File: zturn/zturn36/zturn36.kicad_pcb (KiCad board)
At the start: 4 copper layers, 189.9 x 136.5 mm, 61 parts, among them J11 Conn_02x40_Odd_Even, J12 Conn_02x40_Odd_Even, J5V1 Conn_01x03, Q1 SSM6N15AFU, Q2 SSM6N15AFU, Q3 SSM6N15AFU, Q4 SSM6N15AFU, Q5 SSM6N15AFU, Q6 SSM6N15AFU, Q7 SSM6N15AFU, Q8 SSM6N15AFU, Q9 SSM6N15AFU, U1 74AXP4T245, U10 74AXP4T245, U11 74AXP4T245, U12 74AXP4T245, U13 74AXP4T245, U14 LM3940_TO220, U2 74AXP4T245, U3 74AXP4T245, U8 74AXP4T245, U9 74AXP4T245

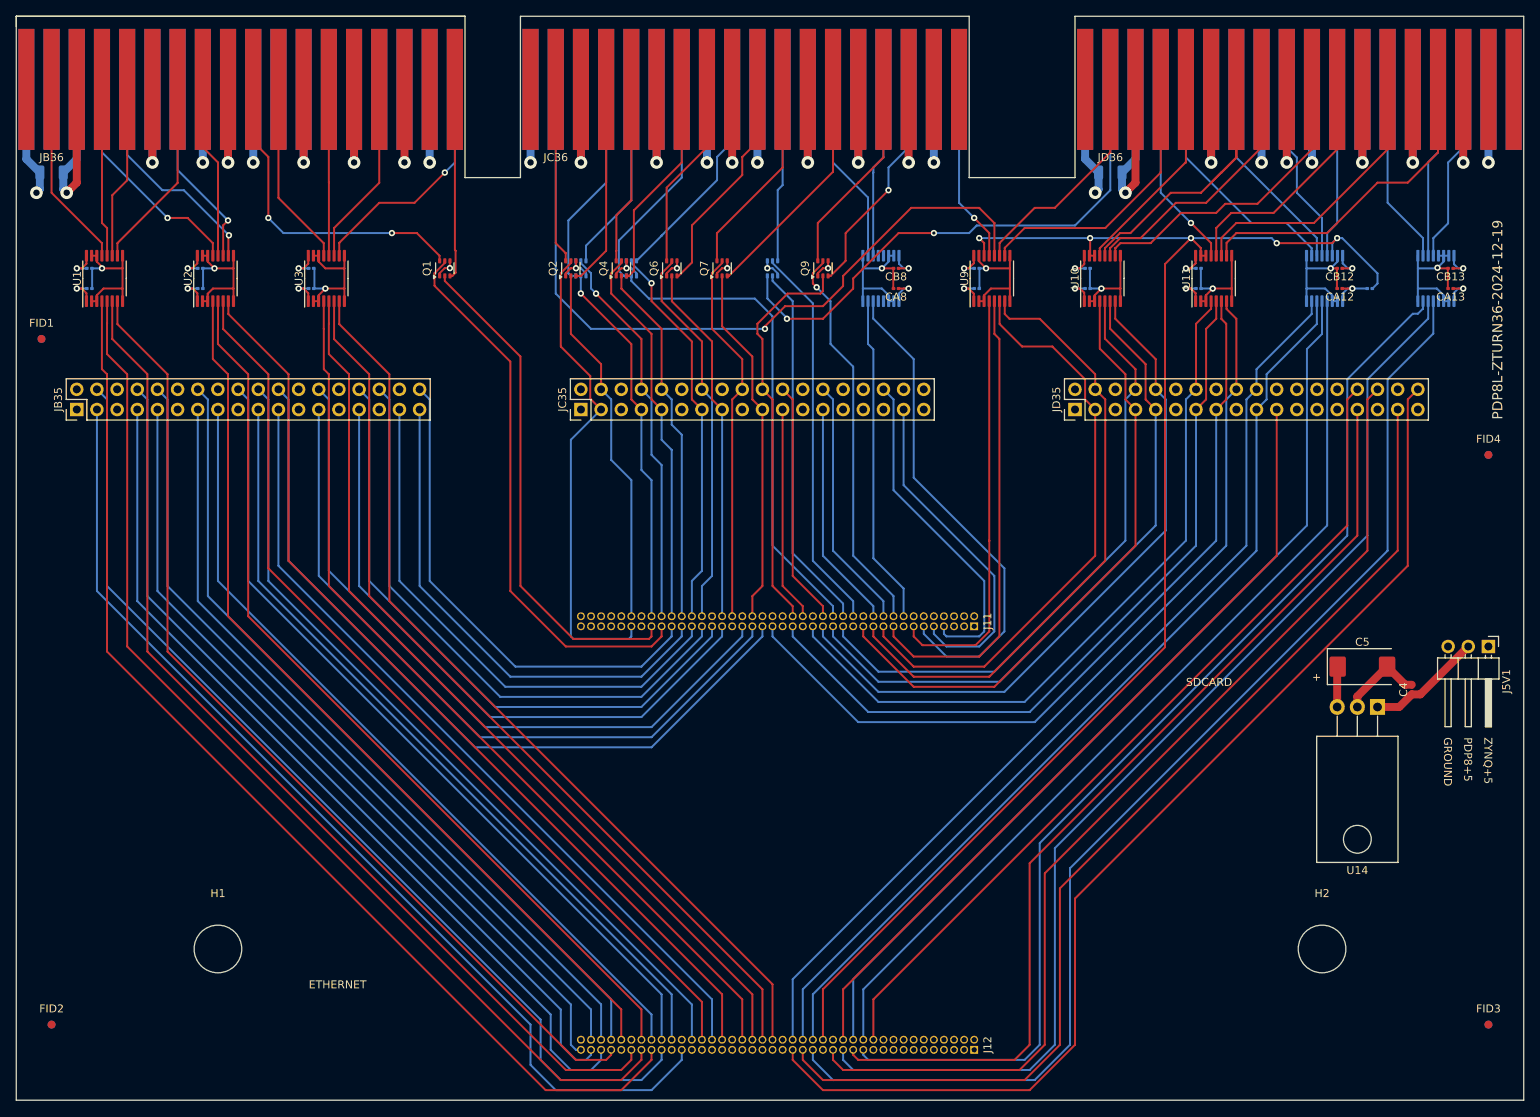
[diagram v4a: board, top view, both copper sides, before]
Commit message: update signals and zturn pcbs with pullups
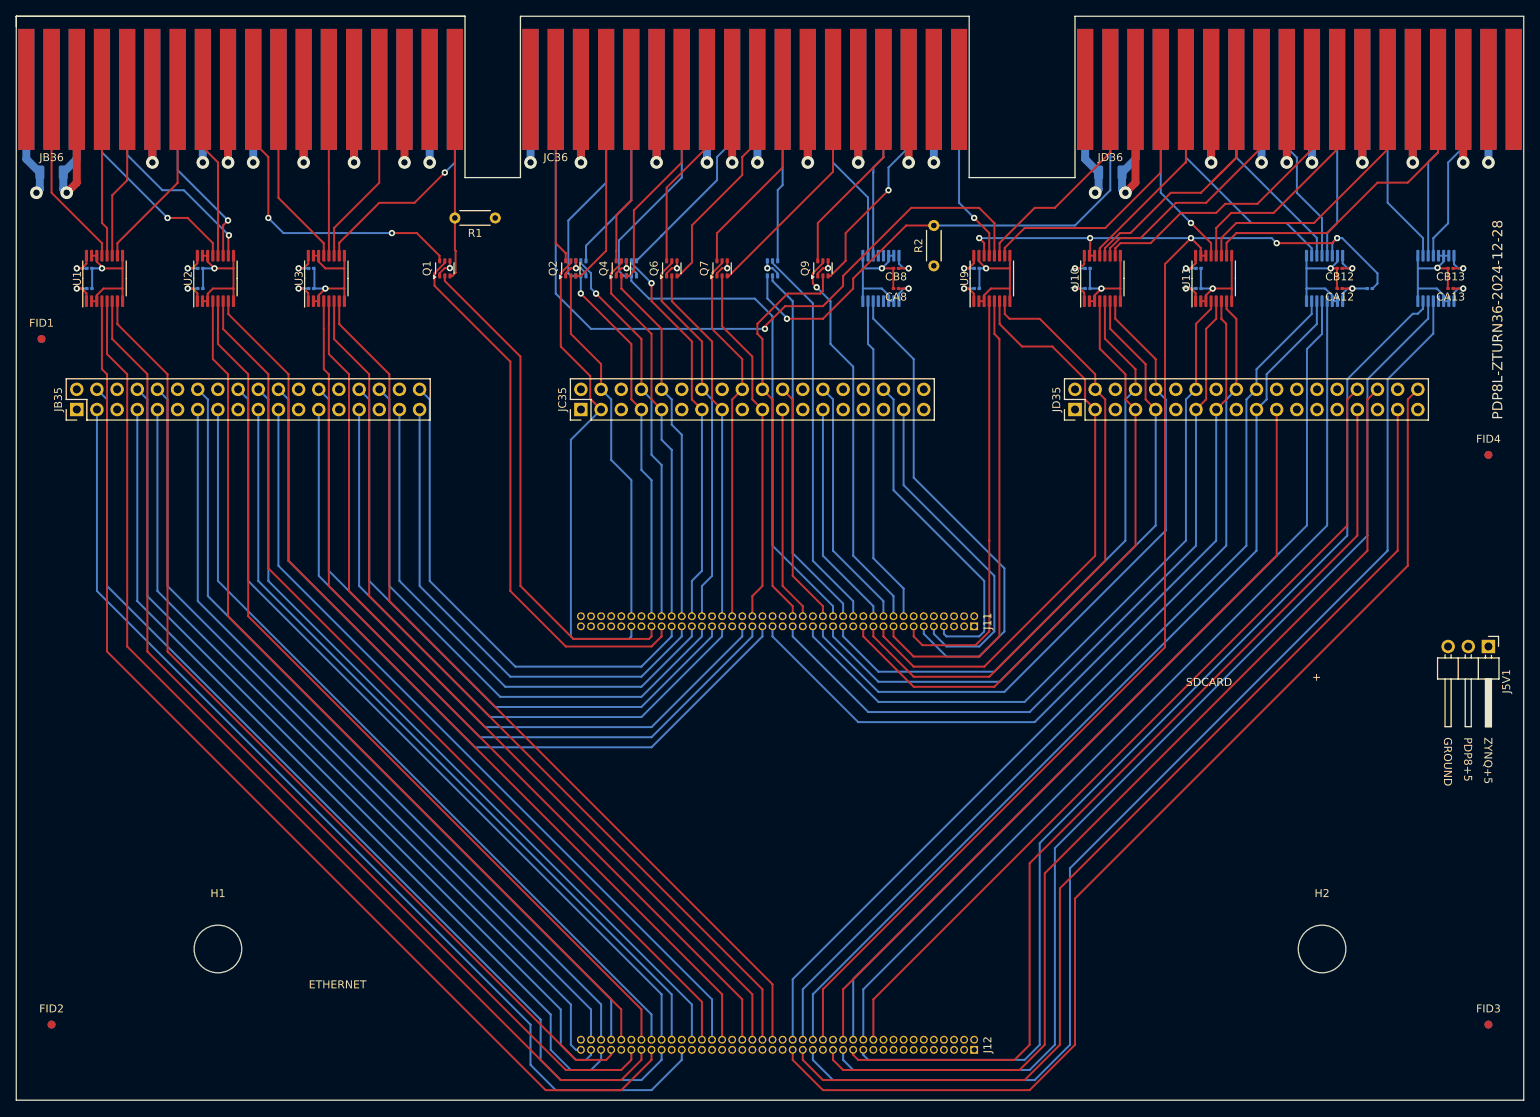
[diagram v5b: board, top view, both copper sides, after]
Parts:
- removed C4: 0.47u, Capacitor_SMD:C_0201_0603Metric
- removed C5: 33u, Capacitor_Tantalum_SMD:CP_EIA-7343-31_Kemet-D
- removed U14: LM3940_TO220, Package_TO_SOT_THT:TO-220-3_Horizontal_TabDown
- added R1: 1K, Resistor_THT:R_Axial_DIN0204_L3.6mm_D1.6mm_P5.08mm_Horizontal, F.Cu at (60.3, 25.4)
- added R2: 1K, Resistor_THT:R_Axial_DIN0204_L3.6mm_D1.6mm_P5.08mm_Horizontal, F.Cu at (115.6, 31.4)
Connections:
- J11 pad 3: unconnected-(J11-Pin_3-Pad3) -> +3V3
- J12 pad 3: unconnected-(J12-Pin_3-Pad3) -> +3V3
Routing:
- net GND: track 479.5 -> 459.7 mm
- net +5V: track 136.9 -> 122.3 mm
- net +3V3: track 47.2 -> 39.9 mm
- net /jD36B2: vias 2 -> 1
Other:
- board text added: "PDP8L-ZTURN36-2024-12-28"
- board text removed: "PDP8L-ZTURN36-2024-12-19"

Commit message: add I2C circuit to zturn boardset to operate front panel board
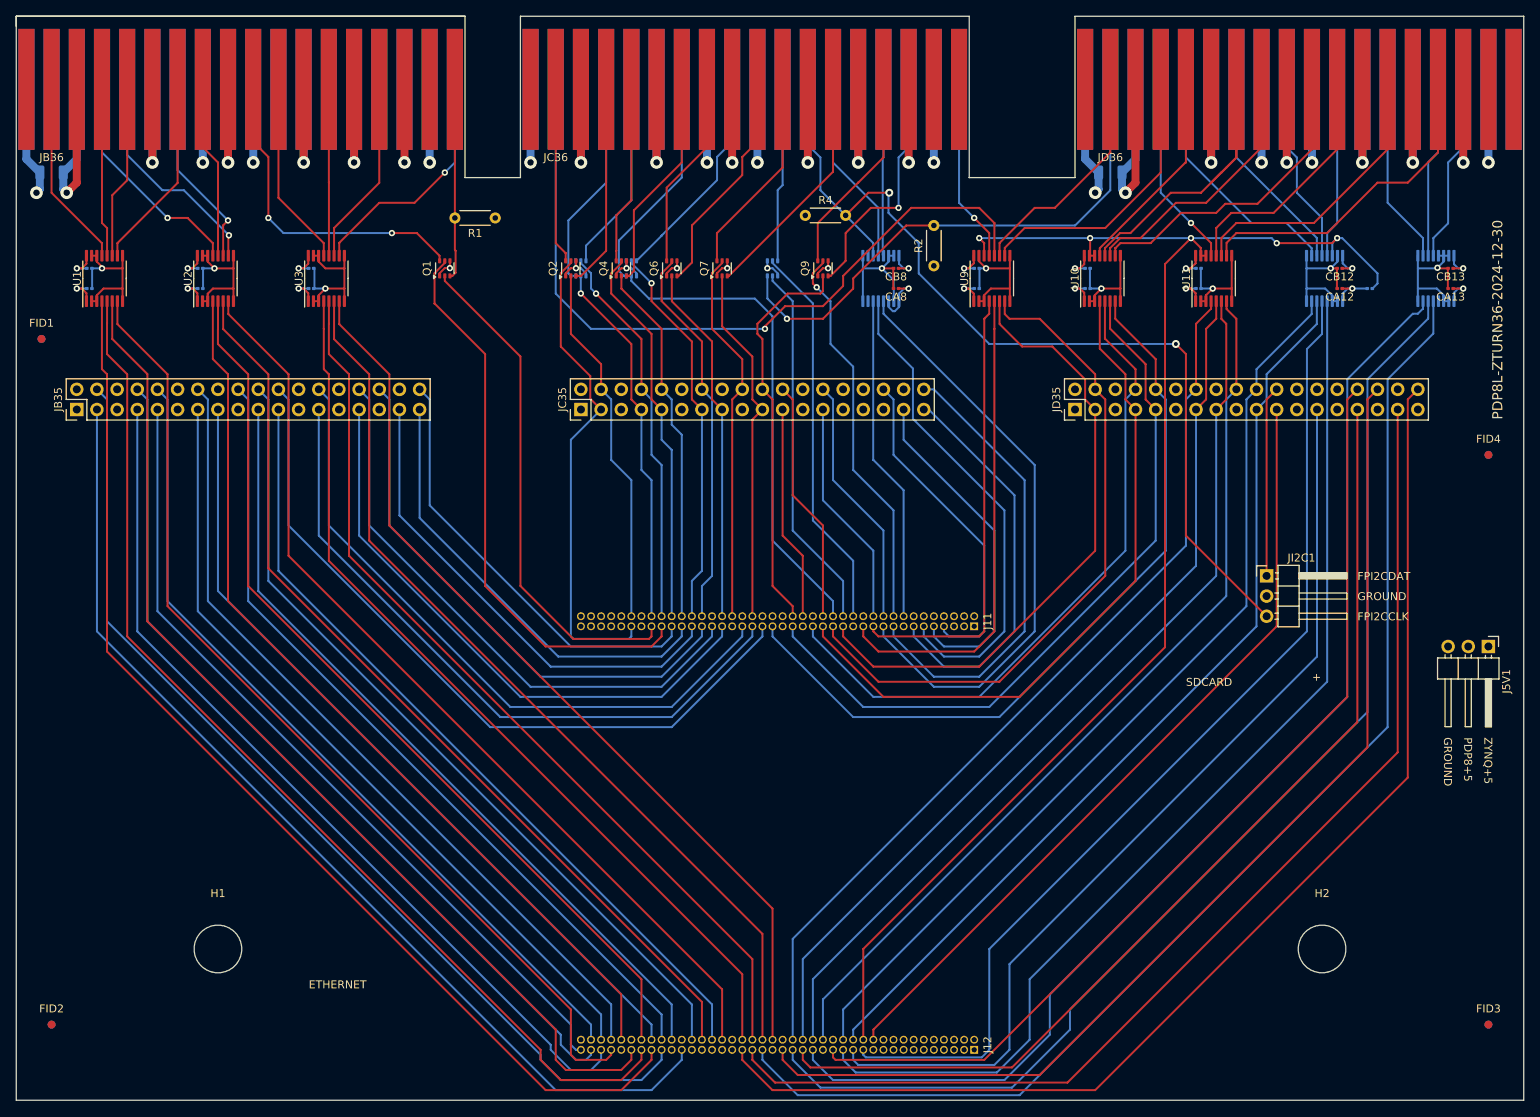
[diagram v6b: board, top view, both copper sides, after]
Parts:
- added JI2C1: Conn_01x03, Connector_PinHeader_2.54mm:PinHeader_1x03_P2.54mm_Horizontal, F.Cu at (157.5, 70.5)
- added R4: 1K, Resistor_THT:R_Axial_DIN0204_L3.6mm_D1.6mm_P5.08mm_Horizontal, F.Cu at (99.4, 25.1)
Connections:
- J11 pad 11: /o_ADDR_ACCEPT -> /o_B_BREAK
- J11 pad 13: /oBUSINIT -> /FPI2CDDIR
- J11 pad 16: /o_B_BREAK -> /FPI2CCLK
- J11 pad 17: /oC36B2 -> /FPI2CDATA
- J11 pad 19: /PIOBUSA -> /o_ADDR_ACCEPT
- J11 pad 21: /PIOBUSH -> /oBUSINIT
- J11 pad 23: /PIOBUSB -> /oC36B2
- J11 pad 27: /PIOBUSJ -> /PIOBUSA
- J11 pad 29: /PIOBUSC -> /PIOBUSH
- J11 pad 31: /PIOBUSK -> /PIOBUSB
- J11 pad 33: /PIOBUSL -> /PIOBUSJ
- J11 pad 37: /PIOBUSD -> /PIOBUSC
- J11 pad 41: /PIOBUSE -> /PIOBUSK
- J12 pad 22: /iIO_SKIP -> /x_INPUTBUS
- J12 pad 23: /oBIOP4 -> /oBIOP1
- J12 pad 24: /oBIOP2 -> /r_BAC
- J12 pad 25: /r_BMB -> /FPI2CDENA
- J12 pad 26: /oBIOP1 -> /PIOBUSF
- J12 pad 27: /oBTS_3 -> /oBIOP2
- J12 pad 28: /x_INPUTBUS -> /PIOBUSN
- J12 pad 29: /iINT_RQST -> /iIO_SKIP
- J12 pad 32: /r_BAC -> /PIOBUSM
- J12 pad 33: /oBTS_1 -> /oBIOP4
- J12 pad 34: /PIOBUSF -> /PIOBUSE
- J12 pad 35: /iAC_CLEAR -> /r_BMB
- J12 pad 36: /PIOBUSN -> /PIOBUSD
- J12 pad 37: /oB_RUN -> /oBTS_3
- J12 pad 38: /PIOBUSM -> /PIOBUSL
- J12 pad 39: unconnected-(J12-Pin_39-Pad39) -> /iINT_RQST
- J12 pad 43: unconnected-(J12-Pin_43-Pad43) -> /oBTS_1
- J12 pad 45: unconnected-(J12-Pin_45-Pad45) -> /iAC_CLEAR
- J12 pad 47: unconnected-(J12-Pin_47-Pad47) -> /oB_RUN
- JC35 pad 35: /i_EXTDMAADD_14 -> /FPI2CDDIR
- JC35 pad 36: /i_EXTDMAADD_13 -> /FPI2CDATA
- JC36 pad N2: GND -> /EPI2CCLK
- JD35 pad 22: unconnected-(JD35-Pin_22-Pad22) -> /EPI2CDAT
- JD35 pad 25: unconnected-(JD35-Pin_25-Pad25) -> /FPI2CDENA
- U8 pad 10: /p_B_BREAK -> unconnected-(U8-2B2-Pad10)
- U8 pad 11: /p_ADDR_ACCEPT -> /EPI2CCLK
- U8 pad 12: unconnected-(U8-1B2-Pad12) -> /p_B_BREAK
- U8 pad 13: unconnected-(U8-1B1-Pad13) -> /p_ADDR_ACCEPT
- U8 pad 3: GND -> +3V3
- U8 pad 4: unconnected-(U8-1A1-Pad4) -> /o_ADDR_ACCEPT
- U8 pad 5: unconnected-(U8-1A2-Pad5) -> /o_B_BREAK
- U8 pad 6: /o_ADDR_ACCEPT -> /FPI2CCLK
- U8 pad 7: /o_B_BREAK -> unconnected-(U8-2A2-Pad7)
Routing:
- net /FPI2CDENA: track 0.00 -> 118.7 mm
- net /EPI2CCLK: track 0.00 -> 110.9 mm, vias 0 -> 2
- net /FPI2CDATA: track 0.00 -> 58.7 mm
- net /FPI2CDDIR: track 0.00 -> 49.8 mm
- net /FPI2CCLK: track 0.00 -> 41.3 mm
- net /EPI2CDAT: track 0.00 -> 24.0 mm
- net /PIOBUSL: track 91.6 -> 114.9 mm
- net /o_B_BREAK: track 41.5 -> 62.0 mm
- net /oBIOP2: track 117.2 -> 135.7 mm
- net /PIOBUSD: track 96.5 -> 114.6 mm
- net /iIO_SKIP: track 107.2 -> 124.1 mm
- net /o_ADDR_ACCEPT: track 62.0 -> 75.3 mm
- net /PIOBUSE: track 102.0 -> 114.8 mm
- net /oBIOP1: track 117.5 -> 128.7 mm
- net /oB_RUN: track 141.2 -> 152.4 mm
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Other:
- board text added: "FPI2CCLK"
- board text added: "FPI2CDAT"
- board text added: "PDP8L-ZTURN36-2024-12-30"
- board text removed: "PDP8L-ZTURN36-2024-12-28"

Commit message: fix hizmembus while reading memory and make iMEMINCR active high
at this point:
  looptest testrands works on core and fpga memory
  cmemtest works on fpga memory
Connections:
- net /i_MEMINCR renamed /iMEMINCR
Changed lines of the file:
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@@
   (net 26 "/i_DATA_IN")
   (net 27 "/o_B_BREAK")
-  (net 28 "/i_MEMINCR")
+  (net 28 "/iMEMINCR")
   (net 29 "unconnected-(JD36-PadU1)")
   (net 30 "unconnected-(JD36-PadV1)")
@@
       (net 21 "GND") (pinfunction "S2") (pintype "passive"))
     (pad "5" smd roundrect (at 0.95 0 90) (size 0.65 0.4) (layers "F.Cu" "F.Paste" "F.Mask") (roundrect_rratio 0.25)
-      (net 28 "/i_MEMINCR") (pinfunction "G2") (pintype "passive"))
+      (net 28 "/iMEMINCR") (pinfunction "G2") (pintype "passive"))
     (pad "6" smd roundrect (at 0.95 -0.65 90) (size 0.65 0.4) (layers "F.Cu" "F.Paste" "F.Mask") (roundrect_rratio 0.25)
       (net 71 "/j_DMAADDR_08") (pinfunction "D1") (pintype "passive"))
@@
       (net 207 "/FPI2CDATA") (pinfunction "Pin_17") (pintype "passive"))
     (pad "18" thru_hole oval (at 1.27 -10.16 90) (size 1 1) (drill 0.65) (layers "*.Cu" "*.Mask")
-      (net 28 "/i_MEMINCR") (pinfunction "Pin_18") (pintype "passive"))
+      (net 28 "/iMEMINCR") (pinfunction "Pin_18") (pintype "passive"))
     (pad "19" thru_hole oval (at 0 -11.43 90) (size 1 1) (drill 0.65) (layers "*.Cu" "*.Mask")
       (net 179 "/o_ADDR_ACCEPT") (pinfunction "Pin_19") (pintype "passive"))
